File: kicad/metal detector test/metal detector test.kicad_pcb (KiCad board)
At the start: 2 copper layers, 82.8 x 88.9 mm, 111 parts, among them J1 3.5mm audio jack TRS, Q1 PNP, Q2 NPN, SW0 SW_SPST, SW1 SW_SPST, SW10 SW_SPST, SW2 SW_SPST, SW3 SW_SPST, SW4 SW_SPST, SW5 SW_SPST, SW6 SW_SPST, SW7 SW_SPST, SW8 SW_SPST, U1 op amp (higher voltage), U10 3.3v lin reg, U11 lp filter, U12 op amp (lower voltage), U2 nucleo-32 uC module, U3 9v lin reg, U4 5v lin reg, U5 3.3v lin reg, U6 audio amp, U7 lp filter, U8 switch debounce, U9 5v lin reg

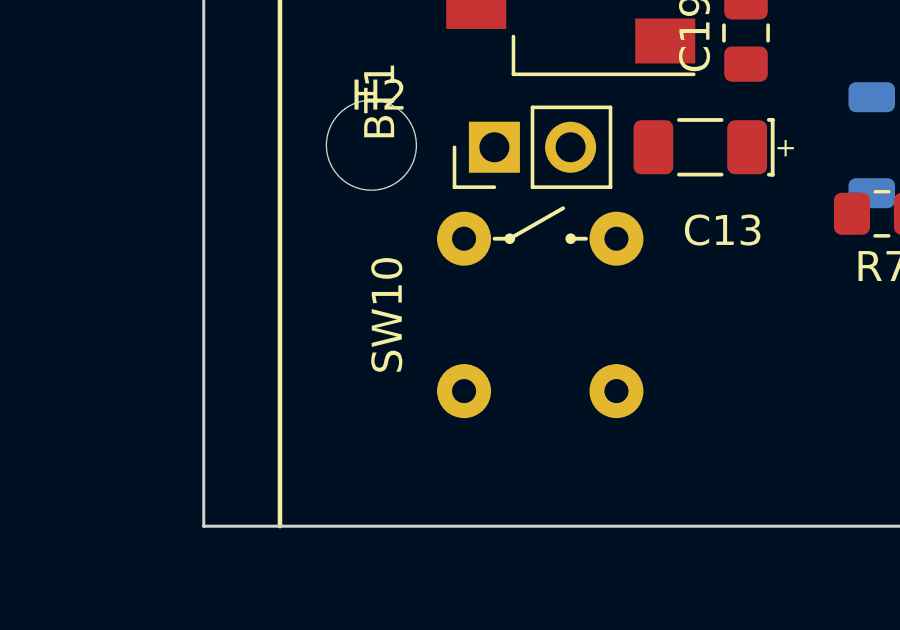
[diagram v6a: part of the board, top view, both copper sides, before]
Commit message: Swapped DAC outputs for better impedance balancing
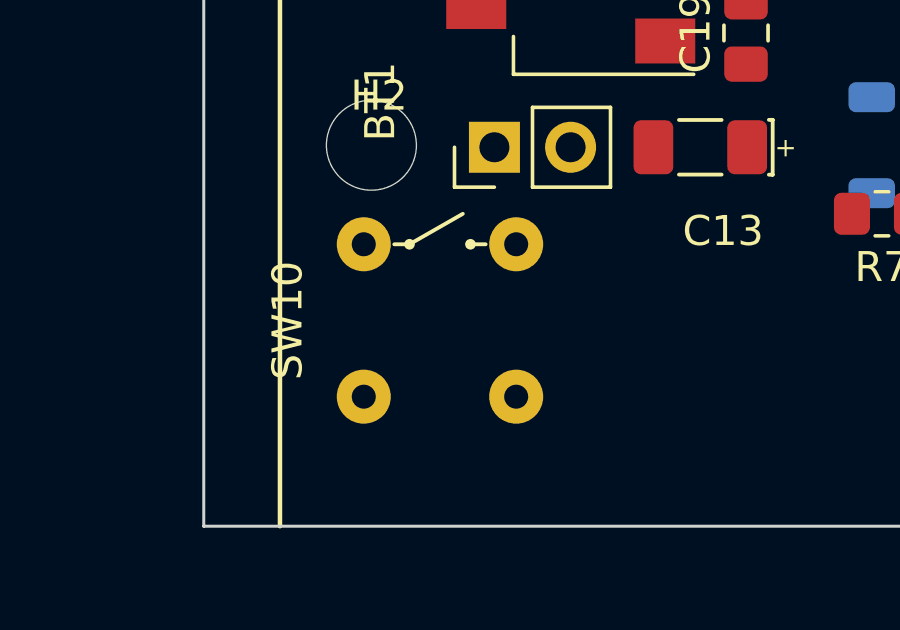
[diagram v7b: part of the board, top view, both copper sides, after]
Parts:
- moved SW10 3.35 mm to (5.33, 79.5)
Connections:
- U2 pad 22: TX_AMP_RAW -> AUDIO
- U2 pad 24: AUDIO -> TX_AMP_RAW
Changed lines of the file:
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@@
   )
   (footprint "allen footprints:A11AH_right_angle_toggle_switch" (layer "F.Cu")
-    (at 8.677 79.3165)
+    (at 5.334 79.502)
     (property "MPN" "A11AH")
     (property "Sheetfile" "metal detector test.kicad_sch")
@@
       (net 41 "SW7") (pinfunction "PA_3") (pintype "bidirectional"))
     (pad "22" thru_hole oval (at 15.24 20.32 180) (size 1.6 1.6) (drill 1) (layers "*.Cu" "*.Mask")
-      (net 42 "TX_AMP_RAW") (pinfunction "PA_4") (pintype "bidirectional"))
+      (net 10 "AUDIO") (pinfunction "PA_4") (pintype "bidirectional"))
     (pad "23" thru_hole oval (at 15.24 17.78 180) (size 1.6 1.6) (drill 1) (layers "*.Cu" "*.Mask")
       (net 65 "Net-(U2-PA_5)") (pinfunction "PA_5") (pintype "bidirectional"))
     (pad "24" thru_hole oval (at 15.24 15.24 180) (size 1.6 1.6) (drill 1) (layers "*.Cu" "*.Mask")
-      (net 10 "AUDIO") (pinfunction "PA_6") (pintype "bidirectional"))
+      (net 42 "TX_AMP_RAW") (pinfunction "PA_6") (pintype "bidirectional"))
     (pad "25" thru_hole oval (at 15.24 12.7 180) (size 1.6 1.6) (drill 1) (layers "*.Cu" "*.Mask")
       (net 23 "TX_OSC_SCALED") (pinfunction "PA_7") (pintype "bidirectional"))

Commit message: About halfway done routing tracks/traces
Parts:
- removed TP3: TX_D_AMP, TestPoint:TestPoint_Pad_D1.5mm
- moved TP6 13.5 mm to (17.0, 40.1)
- moved TP5 5.79 mm to (53.1, 49.5)
- moved C6 5.67 mm to (54.6, 77.0), turned to 90 degrees
- moved TP7 5.00 mm to (23.6, 39.4)
- moved C8 0.51 mm to (42.7, 85.3)
- moved C9 0.51 mm to (42.7, 81.5)
- moved H2 0.41 mm to (5.38, 75.8)
- moved TP8 0.36 mm to (8.13, 51.3)
- moved C23 0.11 mm to (56.4, 68.1)
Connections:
- U2 pad 22: AUDIO -> TX_AMP_RAW
- U2 pad 24: TX_AMP_RAW -> AUDIO
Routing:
- net +BATT: track 0.00 -> 81.0 mm
- net TX_OSC_SCALED: track 0.00 -> 52.2 mm
- net TX_AMP_RAW: track 0.00 -> 50.2 mm
- net +5VA: track 0.00 -> 46.9 mm
- net +9V: track 0.00 -> 34.8 mm
- net AUDIO: track 0.00 -> 34.4 mm, vias 0 -> 2
- net +3.3V: track 0.00 -> 30.5 mm
- net TX_FILTER_CLK: track 0.00 -> 25.7 mm, vias 0 -> 1
- net Net-(JP5-A): track 0.00 -> 24.4 mm, vias 0 -> 2
- net Net-(JP1-B): track 0.00 -> 24.1 mm, vias 0 -> 2
- net RX_FILTER_CLK: track 0.00 -> 23.9 mm
- net +3.3VA: track 0.00 -> 23.1 mm
- net Net-(C24-Pad2): track 0.00 -> 18.4 mm
- net Net-(J1-PadTN): track 0.00 -> 15.2 mm, vias 0 -> 1
- net Net-(C16-Pad1): track 0.00 -> 13.3 mm
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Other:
- copper layers 2 -> 4
